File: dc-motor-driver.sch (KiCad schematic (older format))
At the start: 18 parts, among them J1 BAT, J2 Logic, J3 FL, J4 RL, J5 FR, J6 RR, J7 Power, Q1 IRF7303, Q2 IRF7303

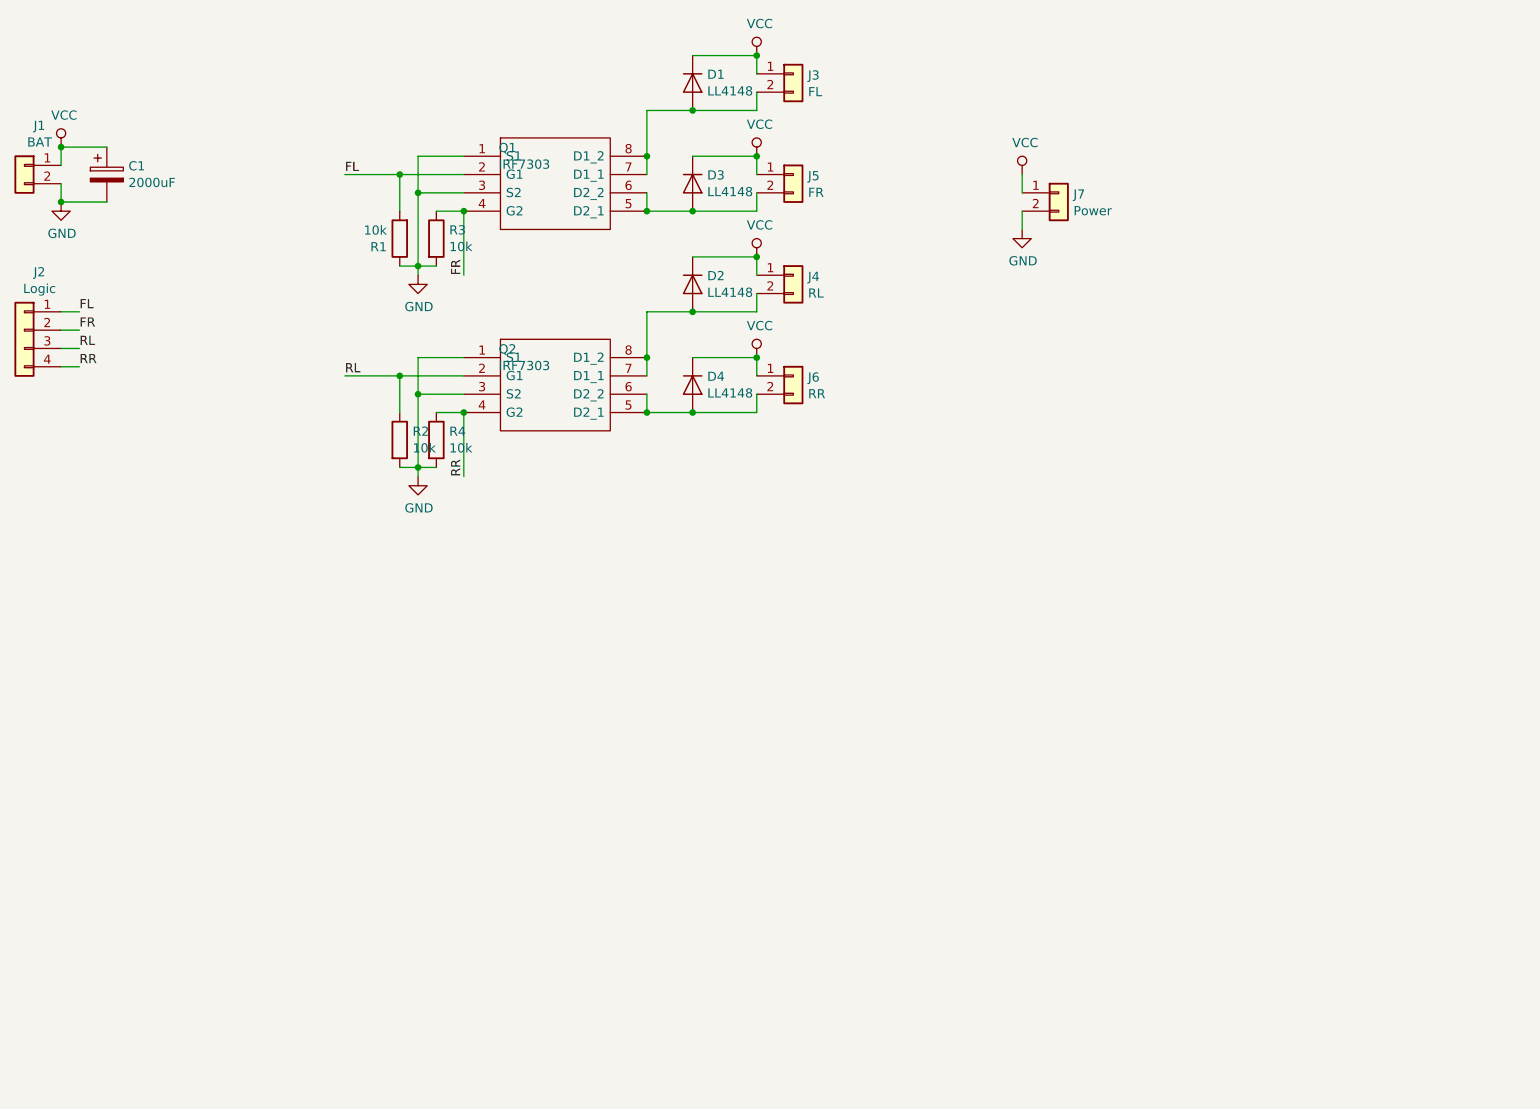
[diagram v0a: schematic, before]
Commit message: Redesigned the board to work with TTGO T7 modules.
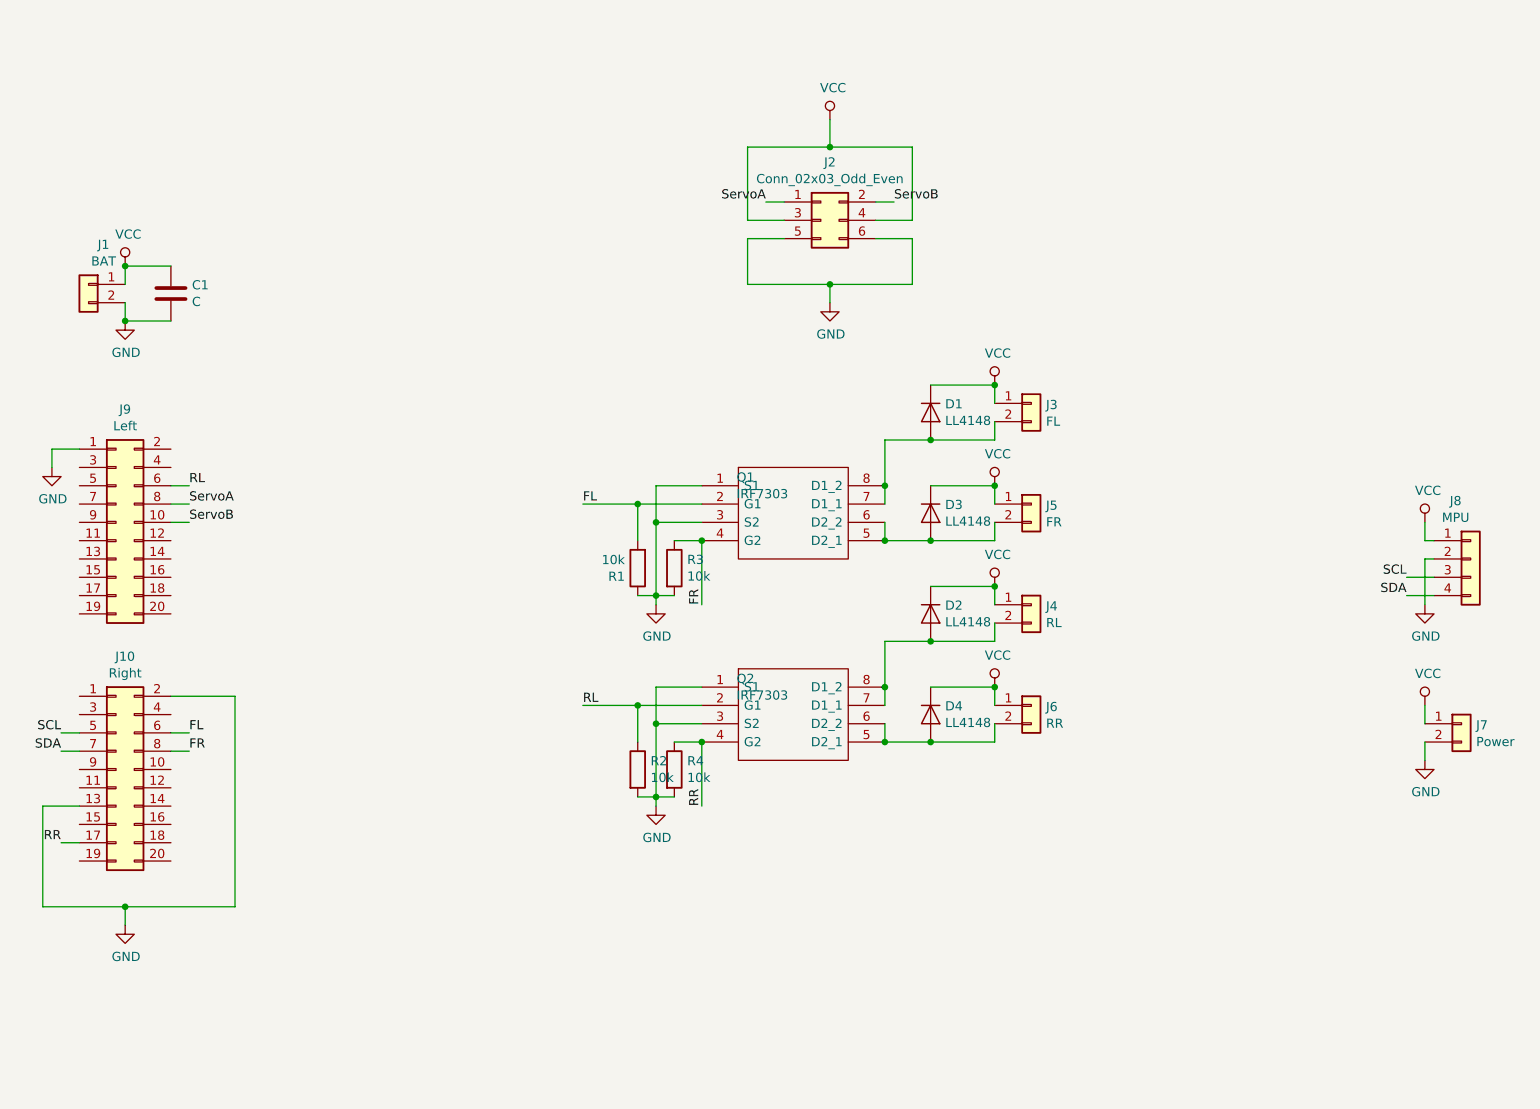
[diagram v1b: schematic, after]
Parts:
- removed C1: 2000uF, Capacitor_SMD:CP_Elec_6.3x5.9, symbol Device:CP
- removed J2: Logic, Connector_PinHeader_2.54mm:PinHeader_1x04_P2.54mm_Vertical, symbol Connector_Generic:Conn_01x04
- added C1: C, Capacitor_Tantalum_SMD:CP_EIA-3528-21_Kemet-B_Pad1.50x2.35mm_HandSolder, symbol Device:C
- added J10: Right, Connector_PinHeader_2.54mm:PinHeader_2x10_P2.54mm_Vertical, symbol Connector_Generic:Conn_02x10_Odd_Even
- added J2: Conn_02x03_Odd_Even, Connector_PinHeader_2.54mm:PinHeader_2x03_P2.54mm_Vertical, symbol Connector_Generic:Conn_02x03_Odd_Even
- added J8: MPU, Connector_PinHeader_2.54mm:PinHeader_1x04_P2.54mm_Vertical, symbol Connector_Generic:Conn_01x04
- added J9: Left, Connector_PinHeader_2.54mm:PinHeader_2x10_P2.54mm_Vertical, symbol Connector_Generic:Conn_02x10_Odd_Even
- J3, J4, J5, J6: footprint Connector_PinHeader_2.00mm:PinHeader_1x02_P2.00mm_Vertical -> Connector_Molex:Molex_PicoBlade_53261-0271_1x02-1MP_P1.25mm_Horizontal
- J7: footprint Connector_PinHeader_2.00mm:PinHeader_1x02_P2.00mm_Vertical -> Connector_PinHeader_2.54mm:PinHeader_1x02_P2.54mm_Vertical
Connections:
- net FL: now also J10.6 (Pin_6)
- net FR: now also J10.8 (Pin_8)
- net GND: now also C1.2, J10.13 (Pin_13), J10.2 (Pin_2), J2.5 (Pin_5), J2.6 (Pin_6), J8.2 (Pin_2), J9.1 (Pin_1)
- net RL: now also J9.6 (Pin_6)
- net RR: now also J10.17 (Pin_17)
- net VCC: now also C1.1, J2.3 (Pin_3), J2.4 (Pin_4), J8.1 (Pin_1)
- new net SCL: J10.5 (Pin_5), J8.3 (Pin_3)
- new net SDA: J10.7 (Pin_7), J8.4 (Pin_4)
- new net ServoA: J2.1 (Pin_1), J9.8 (Pin_8)
- new net ServoB: J2.2 (Pin_2), J9.10 (Pin_10)
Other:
- moved on the sheet: D1, D2, D3, D4, J1, J3, J4, J5, J6, J7, Q1, Q2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

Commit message: Added a third servo and an LED.
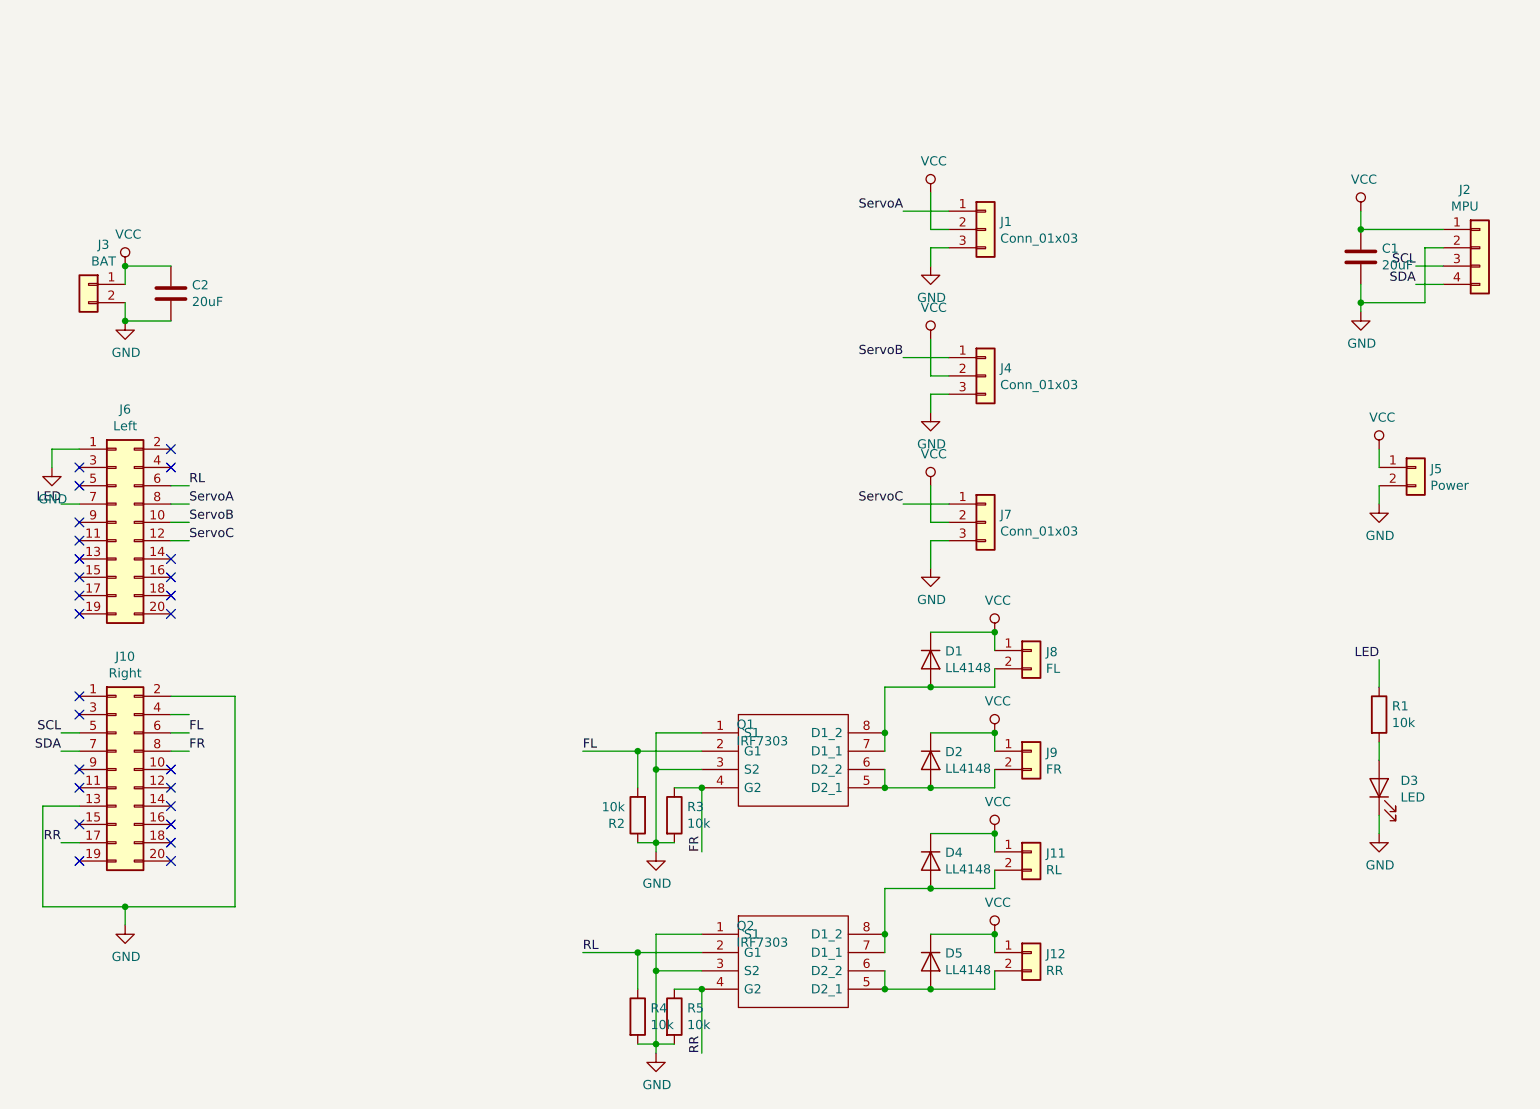
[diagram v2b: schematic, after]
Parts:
- removed J2: Conn_02x03_Odd_Even, Connector_PinHeader_2.54mm:PinHeader_2x03_P2.54mm_Vertical, symbol Connector_Generic:Conn_02x03_Odd_Even
- added C1: 20uF, Capacitor_SMD:C_1206_3216Metric_Pad1.42x1.75mm_HandSolder, symbol Device:C
- added D3: LED, LED_SMD:LED_1206_3216Metric_Pad1.42x1.75mm_HandSolder, symbol Device:LED
- added J1, J4, J7: Conn_01x03, Connector_PinHeader_2.54mm:PinHeader_1x03_P2.54mm_Vertical, symbol Connector_Generic:Conn_01x03
- added R1: 10k, Resistor_SMD:R_1206_3216Metric, symbol Device:R
- C2: renamed from C1; value C -> 20uF
- renumbered D3 to D2, D2 to D4, D4 to D5, J4 to J11, J6 to J12, J8 to J2, J1 to J3, J7 to J5, J9 to J6, J3 to J8, J5 to J9, R1 to R2, R2 to R4, R4 to R5
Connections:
- net GND: now also C1.2, D3.1 (K), J1.3 (Pin_3), J4.3 (Pin_3), J7.3 (Pin_3)
- net ServoA: now also J1.1 (Pin_1)
- net ServoB: now also J4.1 (Pin_1)
- net VCC: now also C1.1, J1.2 (Pin_2), J4.2 (Pin_2), J7.2 (Pin_2)
- net ServoC: now reaches J6.12 (Pin_12)
- net ServoC: now also J7.1 (Pin_1)
- net LED: now reaches J6.7 (Pin_7)
- net LED: now also R1.1
- new net: D3.2 (A), R1.2
- no-connect marks 0 -> 26
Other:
- moved on the sheet: D1, D2, D4, D5, J11, J12, J2, J5, J8, J9, Q1, Q2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

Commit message: Changed the molex connectors to the vertical version.
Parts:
- J11, J12, J8, J9: footprint Connector_Molex:Molex_PicoBlade_53261-0271_1x02-1MP_P1.25mm_Horizontal -> Connector_Molex:Molex_PicoBlade_53398-0271_1x02-1MP_P1.25mm_Vertical
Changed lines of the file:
@@
 F 0 "J12" H 7180 5792 50  0000 L CNN
 F 1 "RR" H 7180 5701 50  0000 L CNN
-F 2 "Connector_Molex:Molex_PicoBlade_53261-0271_1x02-1MP_P1.25mm_Horizontal" H 7100 5800 50  0001 C CNN
+F 2 "Connector_Molex:Molex_PicoBlade_53398-0271_1x02-1MP_P1.25mm_Vertical" H 7100 5800 50  0001 C CNN
 F 3 "~" H 7100 5800 50  0001 C CNN
 	1    7100 5800
@@
 F 0 "J9" H 7180 4692 50  0000 L CNN
 F 1 "FR" H 7180 4601 50  0000 L CNN
-F 2 "Connector_Molex:Molex_PicoBlade_53261-0271_1x02-1MP_P1.25mm_Horizontal" H 7100 4700 50  0001 C CNN
+F 2 "Connector_Molex:Molex_PicoBlade_53398-0271_1x02-1MP_P1.25mm_Vertical" H 7100 4700 50  0001 C CNN
 F 3 "~" H 7100 4700 50  0001 C CNN
 	1    7100 4700
@@
 F 0 "J11" H 7180 5242 50  0000 L CNN
 F 1 "RL" H 7180 5151 50  0000 L CNN
-F 2 "Connector_Molex:Molex_PicoBlade_53261-0271_1x02-1MP_P1.25mm_Horizontal" H 7100 5250 50  0001 C CNN
+F 2 "Connector_Molex:Molex_PicoBlade_53398-0271_1x02-1MP_P1.25mm_Vertical" H 7100 5250 50  0001 C CNN
 F 3 "~" H 7100 5250 50  0001 C CNN
 	1    7100 5250
@@
 F 0 "J8" H 7180 4142 50  0000 L CNN
 F 1 "FL" H 7180 4051 50  0000 L CNN
-F 2 "Connector_Molex:Molex_PicoBlade_53261-0271_1x02-1MP_P1.25mm_Horizontal" H 7100 4150 50  0001 C CNN
+F 2 "Connector_Molex:Molex_PicoBlade_53398-0271_1x02-1MP_P1.25mm_Vertical" H 7100 4150 50  0001 C CNN
 F 3 "~" H 7100 4150 50  0001 C CNN
 	1    7100 4150

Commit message: Made the battery connector horizontal.
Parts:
- J3: footprint Connector_JST:JST_XH_B2B-XH-A_1x02_P2.50mm_Vertical -> Connector_JST:JST_XH_S2B-XH-A-1_1x02_P2.50mm_Horizontal
- R1: value 10k -> 1k
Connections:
- net GND: now also J3.1 (Pin_1); no longer J3.2 (Pin_2)
- net VCC: now also J3.2 (Pin_2); no longer J3.1 (Pin_1)
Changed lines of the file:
@@
 L Connector_Generic:Conn_01x02 J3
 U 1 1 5DB9E165
-P 1950 2150
-F 0 "J3" H 1868 2367 50  0000 C CNN
-F 1 "BAT" H 1868 2276 50  0000 C CNN
-F 2 "Connector_JST:JST_XH_B2B-XH-A_1x02_P2.50mm_Vertical" H 1950 2150 50  0001 C CNN
-F 3 "~" H 1950 2150 50  0001 C CNN
-	1    1950 2150
-	-1   0    0    -1
+P 1950 2250
+F 0 "J3" H 1868 2467 50  0000 C CNN
+F 1 "BAT" H 1868 2376 50  0000 C CNN
+F 2 "Connector_JST:JST_XH_S2B-XH-A-1_1x02_P2.50mm_Horizontal" H 1950 2250 50  0001 C CNN
+F 3 "~" H 1950 2250 50  0001 C CNN
+	1    1950 2250
+	-1   0    0    1
 $EndComp
 Wire Wire Line
@@
 P 9000 4500
 F 0 "R1" H 9070 4546 50  0000 L CNN
-F 1 "10k" H 9070 4455 50  0000 L CNN
+F 1 "1k" H 9070 4455 50  0000 L CNN
 F 2 "Resistor_SMD:R_1206_3216Metric" V 8930 4500 50  0001 C CNN
 F 3 "~" H 9000 4500 50  0001 C CNN

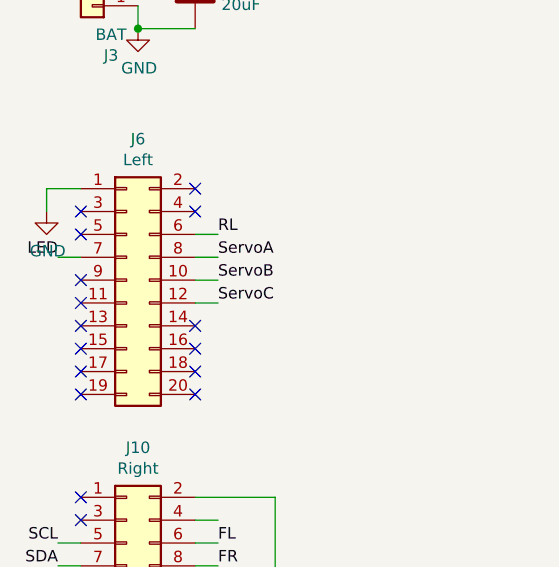
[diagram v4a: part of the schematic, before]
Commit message: Moved servos & led pins to output-enabled pins.
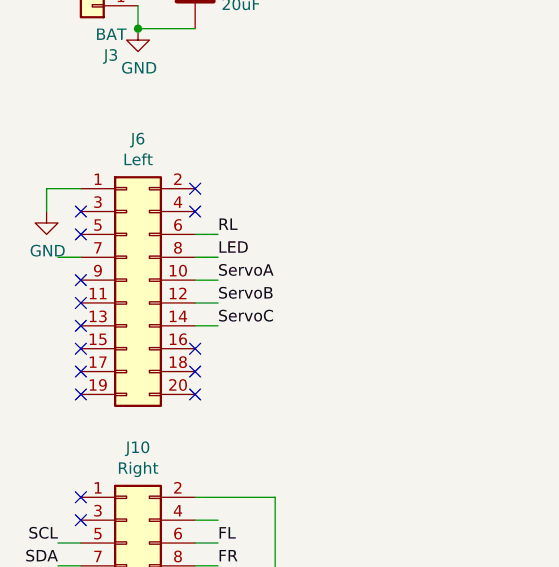
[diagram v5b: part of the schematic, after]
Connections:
- net LED: now also J6.8 (Pin_8); no longer J6.7 (Pin_7)
- net ServoA: now also J6.10 (Pin_10); no longer J6.8 (Pin_8)
- net ServoB: now also J6.12 (Pin_12); no longer J6.10 (Pin_10)
- net ServoC: now also J6.14 (Pin_14); no longer J6.12 (Pin_12)
- no-connect marks 26 -> 25
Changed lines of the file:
@@
 Text Label 2500 4600 0    50   ~ 0
 FL
-Text Label 2500 3350 0    50   ~ 0
+Text Label 2500 3450 0    50   ~ 0
 ServoA
-Text Label 2500 3450 0    50   ~ 0
+Text Label 2500 3550 0    50   ~ 0
 ServoB
 Wire Wire Line
@@
 Wire Wire Line
 	6650 1750 6400 1750
-Text Label 2500 3550 0    50   ~ 0
+Text Label 2500 3650 0    50   ~ 0
 ServoC
 Wire Wire Line
@@
 	1    0    0    -1
 $EndComp
-$Comp
-L power:GND #PWR017
-U 1 1 5E0E8C25
-P 9000 5150
-F 0 "#PWR017" H 9000 4900 50  0001 C CNN
-F 1 "GND" H 9005 4977 50  0000 C CNN
-F 2 "" H 9000 5150 50  0001 C CNN
-F 3 "" H 9000 5150 50  0001 C CNN
-	1    9000 5150
-	1    0    0    -1
-$EndComp
 Text Label 9000 4200 2    50   ~ 0
 LED
@@
 Wire Wire Line
 	9000 4350 9000 4200
-Text Label 1800 3350 2    50   ~ 0
+Text Label 2500 3350 0    50   ~ 0
 LED
 Wire Wire Line
@@
 NoConn ~ 1900 3150
 NoConn ~ 2400 3150
-NoConn ~ 2400 3650
 NoConn ~ 2400 3750
 NoConn ~ 2400 3850
@@
 Wire Wire Line
 	1900 3350 1800 3350
+$Comp
+L power:GND #PWR0101
+U 1 1 5DF1A818
+P 9000 5150
+F 0 "#PWR0101" H 9000 4900 50  0001 C CNN
+F 1 "GND" H 9005 4977 50  0000 C CNN
+F 2 "" H 9000 5150 50  0001 C CNN
+F 3 "" H 9000 5150 50  0001 C CNN
+	1    9000 5150
+	1    0    0    -1
+$EndComp
+Wire Wire Line
+	2400 3650 2500 3650
 $EndSCHEMATC
